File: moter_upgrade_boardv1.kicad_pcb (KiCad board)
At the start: 2 copper layers, 55 parts, among them J2 Conn_01x03_Socket, J3 Conn_01x02_Socket, J4 Conn_01x02_Socket, J5 Conn_01x02_Socket, J6 Conn_01x02_Socket, J7 Conn_ST_STDC14, J8 Conn_01x05_Socket, J9 USB_C_Receptacle_USB2.0_16P, SW1 SW_SPDT, SW2 SW_Push, SW3 SW_Wuerth_450301014042, U1 BD33FC0FP, U2 TLP785, U3 TLP785, U4 STM32H523CCTx, U5 MCP2562-E-P, U6 CH340E, U7 BD33FC0FP

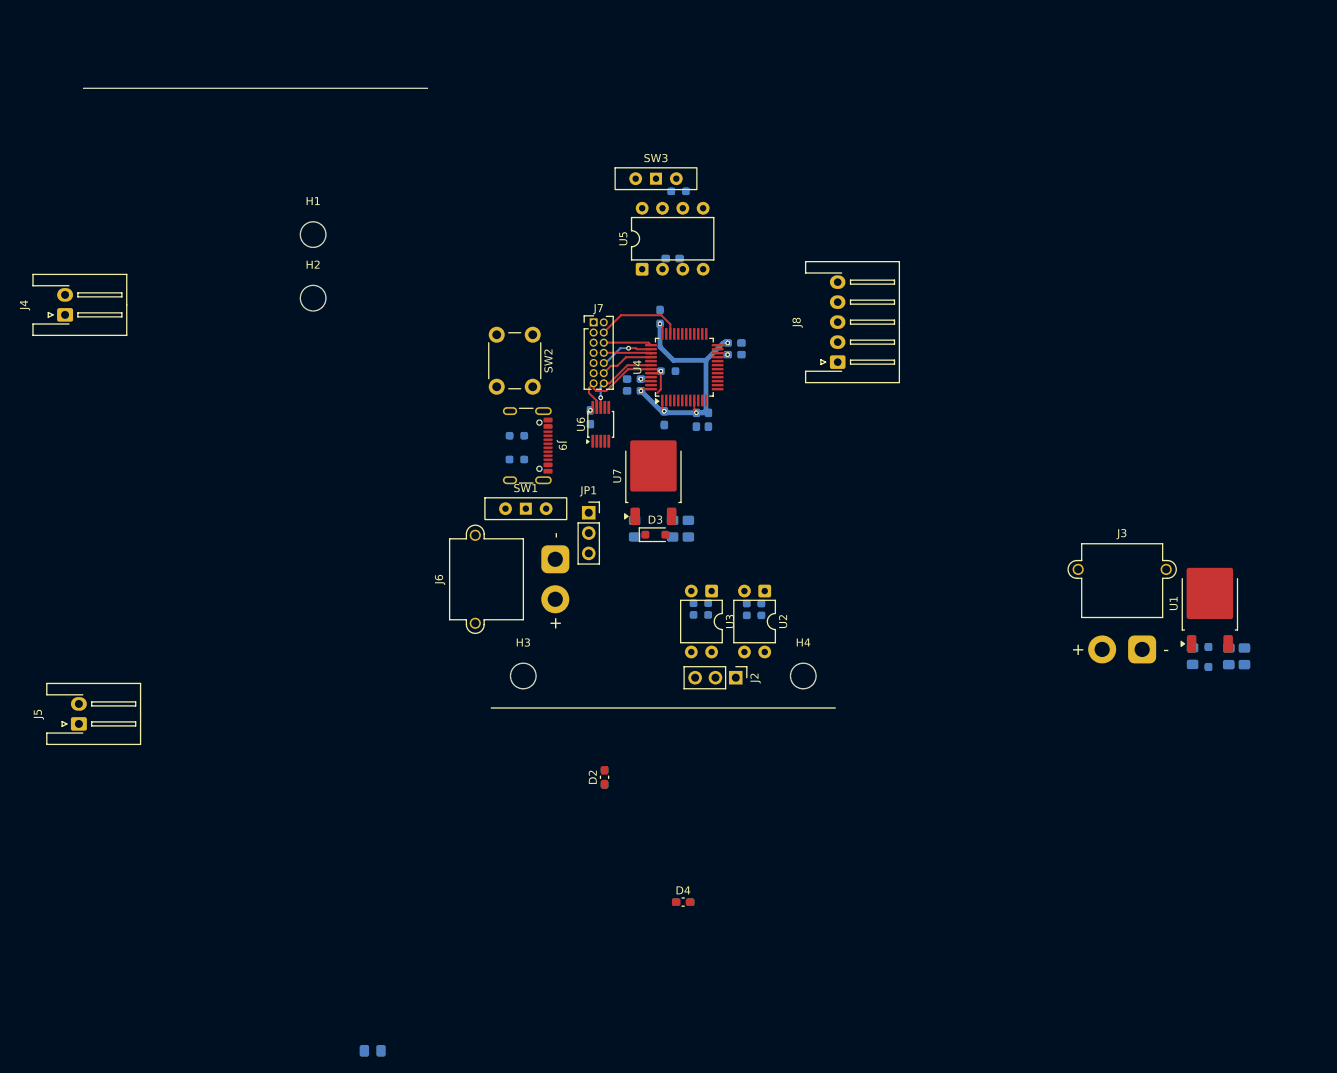
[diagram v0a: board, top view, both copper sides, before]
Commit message: 基本構成の大幅変更(マイコンも変わった
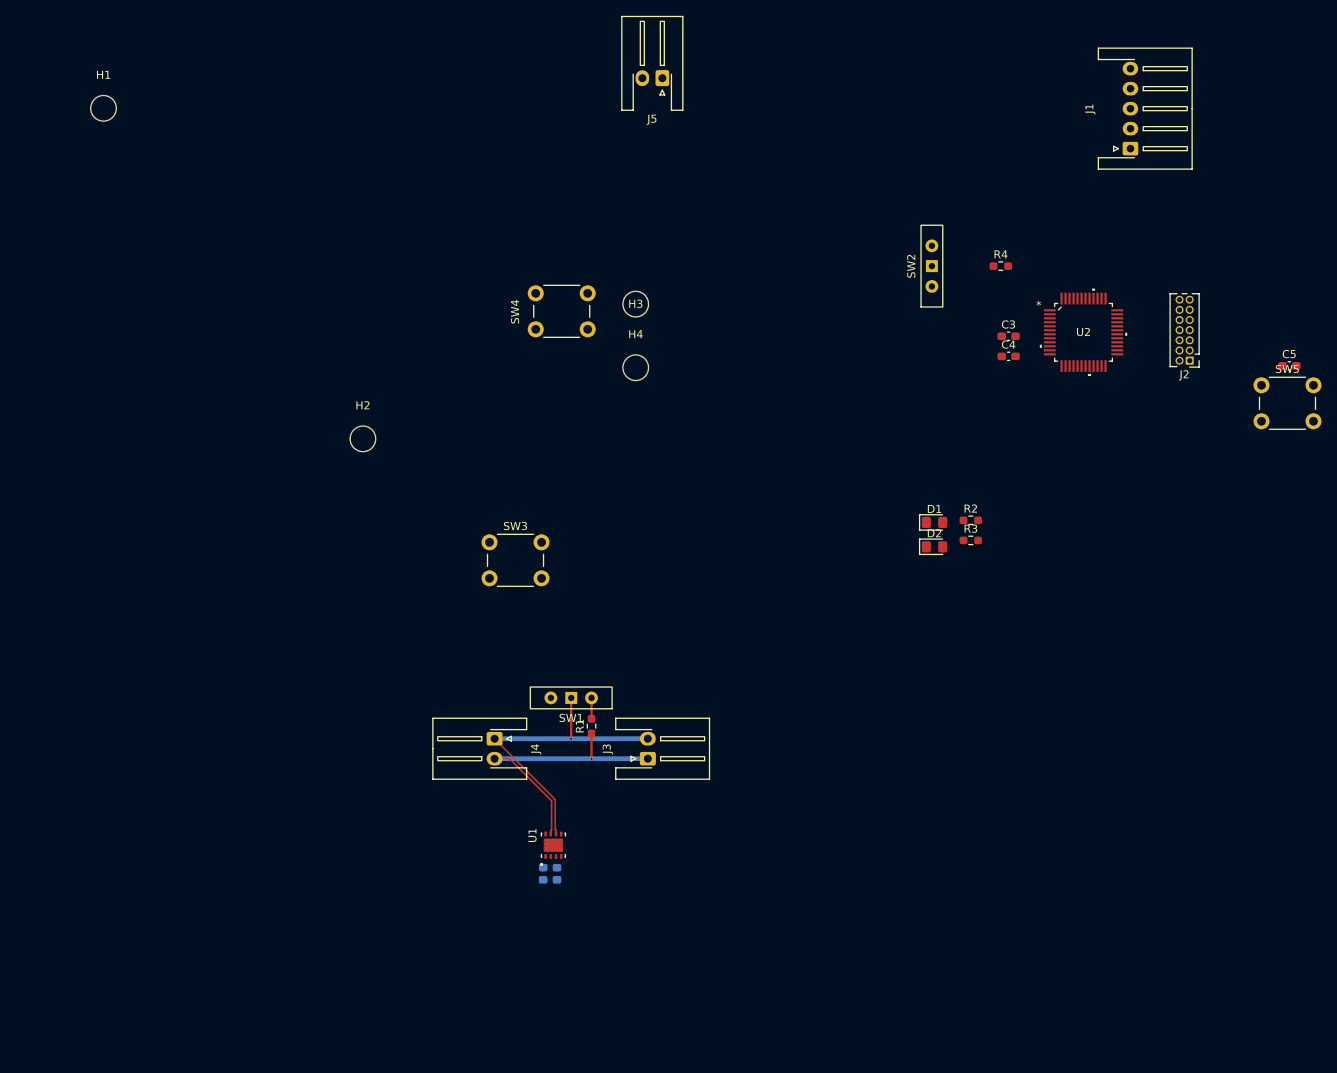
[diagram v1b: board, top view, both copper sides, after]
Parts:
- removed C10, C6, C7, C8: 0.1uF, Capacitor_SMD:C_0603_1608Metric_Pad1.08x0.95mm_HandSolder
- removed C11, C13: 0.1uf, Capacitor_SMD:C_0603_1608Metric_Pad1.08x0.95mm_HandSolder
- removed C12, C14: 1uf, Capacitor_SMD:C_0603_1608Metric_Pad1.08x0.95mm_HandSolder
- removed C15, C16: 4.7μF, Capacitor_SMD:C_0805_2012Metric_Pad1.18x1.45mm_HandSolder
- removed C17: 22μF, Capacitor_SMD:C_0805_2012Metric_Pad1.18x1.45mm_HandSolder
- removed C9: 4.7uf, Capacitor_SMD:C_0805_2012Metric_Pad1.18x1.45mm_HandSolder
- removed D3: D_Shockley, Diode_SMD:D_SOD-323_HandSoldering
- removed D4: LED_RED, Capacitor_SMD:C_0603_1608Metric_Pad1.08x0.95mm_HandSolder
- removed J6: Conn_01x02_Socket, Connector_AMASS:AMASS_XT30PW-M_1x02_P2.50mm_Horizontal
- removed J7: Conn_ST_STDC14, Connector_PinHeader_1.27mm:PinHeader_2x07_P1.27mm_Vertical
- removed J8: Conn_01x05_Socket, Connector_JST:JST_XH_S5B-XH-A-1_1x05_P2.50mm_Horizontal
- removed J9: USB_C_Receptacle_USB2.0_16P, Connector_USB:USB_C_Receptacle_GCT_USB4105-xx-A_16P_TopMnt_Horizontal
- removed JP1: Jumper_3_Bridged12, Connector_PinSocket_2.54mm:PinSocket_1x03_P2.54mm_Vertical
- removed R10, R9: 5.1k, Resistor_SMD:R_0603_1608Metric_Pad0.98x0.95mm_HandSolder
- removed R5: 10K, Resistor_SMD:R_0603_1608Metric_Pad0.98x0.95mm_HandSolder
- removed R6: 120, Resistor_SMD:R_0603_1608Metric_Pad0.98x0.95mm_HandSolder
- removed R7, R8: 1k, Resistor_SMD:R_0603_1608Metric_Pad0.98x0.95mm_HandSolder
- removed U3: TLP785, Package_DIP:DIP-4_W7.62mm
- removed U4: STM32H523CCTx, Package_QFP:LQFP-48_7x7mm_P0.5mm
- removed U5: MCP2562-E-P, Package_DIP:DIP-8_W7.62mm
- removed U6: CH340E, Package_SO:MSOP-10_3x3mm_P0.5mm
- removed U7: BD33FC0FP, Package_TO_SOT_SMD:TO-252-2
- added J1: Conn_01x05_Socket, Connector_JST:JST_XH_S5B-XH-A-1_1x05_P2.50mm_Horizontal, F.Cu at (180.9, 57.5)
- added SW4: SW_Push, Button_Switch_THT:SW_PUSH_6mm, F.Cu at (106.5, 75.6)
- added SW5: SW_Push, Button_Switch_THT:SW_PUSH_6mm, F.Cu at (197.2, 87.1)
- C1: value 4.7μF -> 0.1uF; footprint Capacitor_SMD:C_0805_2012Metric_Pad1.18x1.45mm_HandSolder -> Capacitor_SMD:C_0603_1608Metric_Pad1.08x0.95mm_HandSolder
- C2: value 4.7μF -> 4.7uF; footprint Capacitor_SMD:C_0805_2012Metric_Pad1.18x1.45mm_HandSolder -> Capacitor_SMD:C_0603_1608Metric_Pad1.08x0.95mm_HandSolder
- C3: value 22μF -> 0.1uf; footprint Capacitor_SMD:C_0805_2012Metric_Pad1.18x1.45mm_HandSolder -> Capacitor_SMD:C_0603_1608Metric_Pad1.08x0.95mm_HandSolder; moved to F.Cu
- C4: value 2.2μF -> 1uf; moved to F.Cu
- C5: value 2.2μF -> 0.1uf; moved to F.Cu
- D1: value D_Shockley -> LED_YELLOW; footprint Diode_SMD:D_SOD-323_HandSoldering -> Diode_SMD:D_0805_2012Metric_Pad1.15x1.40mm_HandSolder; moved to F.Cu
- D2: value LED_GREEN -> LED_Green; footprint Capacitor_SMD:C_0603_1608Metric_Pad1.08x0.95mm_HandSolder -> Diode_SMD:D_0805_2012Metric_Pad1.15x1.40mm_HandSolder
- J2: value Conn_01x03_Socket -> Conn_ST_STDC14; footprint Connector_PinHeader_2.54mm:PinHeader_1x03_P2.54mm_Vertical -> Connector_PinHeader_1.27mm:PinHeader_2x07_P1.27mm_Vertical
- J3: footprint Connector_AMASS:AMASS_XT30PW-M_1x02_P2.50mm_Horizontal -> Connector_JST:JST_XH_S2B-XH-A-1_1x02_P2.50mm_Horizontal
- R1: value 68 -> 120; moved to F.Cu
- R2: value 68 -> 1k; moved to F.Cu
- R3: moved to F.Cu
- R4: value 1k -> 10k; moved to F.Cu
- SW1: value SW_SPDT -> SW_Wuerth_450301014042
- SW2: value SW_Push -> SW_SPDT; footprint Button_Switch_THT:SW_PUSH_6mm -> Button_Switch_THT:SW_Slide-03_Wuerth-WS-SLTV_10x2.5x6.4_P2.54mm
- SW3: value SW_Wuerth_450301014042 -> SW_Push; footprint Button_Switch_THT:SW_Slide-03_Wuerth-WS-SLTV_10x2.5x6.4_P2.54mm -> Button_Switch_THT:SW_PUSH_6mm
- U1: value BD33FC0FP -> TCAN3414DRBR; footprint Package_TO_SOT_SMD:TO-252-2 -> TCAN3414DRBR:XCVR_TCAN3414DRBR
- U2: value TLP785 -> STM32C092CBT6; footprint Package_DIP:DIP-4_W7.62mm -> stm32c092cbt6:LQFP48_STM
- moved G*** 112.0 mm to (138.3, 150.3)
- moved J5 108.8 mm to (122.3, 48.7), turned to 180 degrees
- moved C2 89.3 mm to (108.3, 148.9), turned to 0 degrees
- moved U1 87.4 mm to (108.7, 144.6)
- moved C1 84.6 mm to (108.3, 147.4), turned to 0 degrees
- moved C5 81.9 mm to (200.7, 84.7)
- moved J4 75.4 mm to (101.4, 131.3), turned to -90 degrees
- moved J2 69.2 mm to (188.3, 84.0), turned to 180 degrees
- moved J3 63.3 mm to (120.5, 133.8), turned to 90 degrees
- moved R4 56.4 mm to (164.7, 72.2)
- moved U2 51.3 mm to (175.0, 80.5), turned to 0 degrees
- moved SW2 50.6 mm to (156.0, 72.2), turned to 90 degrees
- moved D2 50.3 mm to (156.4, 107.3), turned to 0 degrees
- moved SW3 50.0 mm to (100.8, 106.8)
- moved C3 49.7 mm to (165.6, 81.0), turned to 0 degrees
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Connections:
- C1 pad 1: +24V -> GND
- C1 pad 2: GND1 -> +3.3V
- C2 pad 1: +3V3 -> GND
- C2 pad 2: GND1 -> +3.3V
- C3 pad 1: +3V3 -> +3.3V
- C3 pad 2: GND1 -> GND
- C4 pad 1: GND -> +3.3V
- C4 pad 2: Net-(C4-Pad2) -> GND
- C5 pad 1: GND -> nrst
- C5 pad 2: Net-(C5-Pad2) -> GND
- D1 pad 1: +24V -> Net-(D1-K)
- D1 pad 2: +3V3 -> Net-(D1-A)
- J2 pad 1: Net-(J2-Pin_1) -> unconnected-(J2-NC-Pad1)
- J2 pad 2: Net-(J2-Pin_2) -> unconnected-(J2-NC-Pad2)
- J2 pad 3: GND1 -> +3.3V
- J3 pad 1: GND1 -> CAN1_+
- J3 pad 2: +24V -> CAN1_-
- J4 pad 1: CAN_L -> CAN1_-
- J4 pad 2: CAN_H -> CAN1_+
- J5 pad 1: CAN_L -> GND
- J5 pad 2: CAN_H -> +3.3V
- R1 pad 1: dir to moter -> CAN1_+
- R1 pad 2: Net-(R1-Pad2) -> CAN1R
- R2 pad 1: wm to moter -> GND
- R2 pad 2: Net-(R2-Pad2) -> Net-(D1-K)
- R3 pad 2: Net-(R1-Pad2) -> Net-(D2-K)
- R4 pad 1: GND -> swclk
- R4 pad 2: Net-(R2-Pad2) -> GND
- SW1 pad 1: GND -> CAN1_-
- SW1 pad 2: BOOT0 -> CAN1R
- SW2 pad 1: nrst -> GND
- SW2 pad 2: GND -> BOOT0
- SW3 pad 1: CAN_H -> /ma
- SW3 pad 2: unconnected-(SW3-C-Pad2) -> GND
- U1 pad 1: +24V -> CAN1tx
- U1 pad 2: GND1 -> GND
- U1 pad 3: +3V3 -> +3.3V
- U2 pad 1: Net-(R1-Pad2) -> unconnected-(U2-PC13-Pad1)
- U2 pad 2: GND -> unconnected-(U2-PC14-OSCX_IN-Pad2)
- U2 pad 3: Net-(J2-Pin_1) -> unconnected-(U2-PC15-OSCX_OUT-Pad3)
- U2 pad 4: +3V3 -> unconnected-(U2-PF3-Pad4)
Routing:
- net CAN1_-: track 0.00 -> 39.5 mm, vias 0 -> 1
- net +3.3V: track 37.7 -> 0.00 mm, vias 5 -> 0
- net CAN1_+: track 0.00 -> 36.0 mm, vias 0 -> 1
- net uart1-rx: track 12.7 -> 0.00 mm
- net swdio: track 10.9 -> 0.00 mm
- net uart1-tx: track 10.0 -> 0.00 mm, vias 1 -> 0
- net trst: track 6.73 -> 0.00 mm
- net jtdi: track 6.73 -> 0.00 mm, vias 1 -> 0
- net swclk: track 6.04 -> 0.00 mm
- net swo: track 6.01 -> 0.00 mm
- net BOOT0: track 4.28 -> 0.00 mm, vias 1 -> 0
- net CAN1R: track 0.00 -> 2.54 mm
- net Net-(C5-Pad2): track 1.38 -> 0.00 mm, vias 1 -> 0
- net Net-(C4-Pad2): track 1.33 -> 0.00 mm, vias 1 -> 0
- net Net-(U6-V3): track 0.48 -> 0.00 mm, vias 1 -> 0

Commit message: ver2完成発注(データ同梱)
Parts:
- removed the SW2 at (156.0, 72.2)
- added J6: Conn_01x03_Pin, TerminalBlock_RND:TerminalBlock_RND_205-00233_1x03_P5.08mm_Horizontal, F.Cu at (73.1, 104.0)
- added R5: 10k, Resistor_SMD:R_0805_2012Metric, B.Cu at (77.1, 83.8)
- added R6: 10k, Resistor_SMD:R_0805_2012Metric, B.Cu at (68.4, 84.8)
- added R7: 10k, Resistor_SMD:R_0805_2012Metric, B.Cu at (77.1, 81.9)
- added R8: 10k, Resistor_SMD:R_0805_2012Metric, F.Cu at (95.4, 75.7)
- C3, C4, C5, R1, R2, R3: moved to B.Cu
- R4: footprint Resistor_SMD:R_0603_1608Metric_Pad0.98x0.95mm_HandSolder -> Resistor_SMD:R_0805_2012Metric; moved to B.Cu
- moved C5 139.7 mm to (61.0, 85.1), turned to 90 degrees
- moved SW4 138.0 mm to (59.2, 87.2), turned to 180 degrees
- moved G*** 106.3 mm to (69.8, 69.0)
- moved U2 98.8 mm to (76.2, 81.8)
- moved C4 96.8 mm to (68.8, 82.2), turned to -90 degrees
- moved J1 96.4 mm to (85.0, 67.8), turned to 180 degrees
- moved J2 95.4 mm to (93.3, 75.0), turned to -90 degrees
- moved C3 95.4 mm to (70.3, 82.2), turned to -90 degrees
- moved R4 87.3 mm to (77.6, 78.7), turned to 180 degrees
- moved R3 81.2 mm to (80.0, 100.0)
- moved D2 76.7 mm to (80.0, 100.0), turned to 180 degrees
- moved R2 75.0 mm to (86.0, 100.0)
- moved H3 73.2 mm to (52.5, 107.5)
- moved C2 70.6 mm to (76.9, 85.7), turned to 180 degrees
- moved D1 70.5 mm to (86.0, 100.0), turned to 180 degrees
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- renumbered SW3 to SW2, SW4 to SW3, SW5 to SW4
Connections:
- U2 pad 23: unconnected-(U2-PB11-Pad23) -> Net-(D2-A)
- U2 pad 24: unconnected-(U2-PB12-Pad24) -> Net-(D1-A)
- U2 pad 25: unconnected-(U2-PB13-Pad25) -> /mb
- U2 pad 26: unconnected-(U2-PB14-Pad26) -> /ma
- U2 pad 39: /ma -> unconnected-(U2-PD1-Pad39)
- U2 pad 40: /mb -> unconnected-(U2-PD2-Pad40)
- U2 pad 47: Net-(D1-A) -> unconnected-(U2-PB8-Pad47)
- U2 pad 48: Net-(D2-A) -> unconnected-(U2-PB9-Pad48)
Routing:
- net +3.3V: track 0.00 -> 80.3 mm, vias 0 -> 3
- net GND: track 0.00 -> 58.8 mm, vias 0 -> 85
- net nrst: track 0.00 -> 32.5 mm, vias 0 -> 2
- net /mb: track 0.00 -> 29.5 mm, vias 0 -> 1
- net dir to moter: track 0.00 -> 25.8 mm
- net pwm to moter: track 0.00 -> 25.5 mm
- net swdio: track 0.00 -> 18.3 mm
- net Net-(D1-A): track 0.00 -> 16.5 mm, vias 0 -> 2
- net en-b: track 0.00 -> 15.7 mm
- net Net-(D2-A): track 0.00 -> 14.3 mm
- net /ma: track 0.00 -> 13.6 mm, vias 0 -> 1
- net swclk: track 0.00 -> 13.3 mm, vias 0 -> 1
- net en-a: track 0.00 -> 12.0 mm
- net strx: track 0.00 -> 10.9 mm, vias 0 -> 1
- net sttx: track 0.00 -> 10.1 mm, vias 0 -> 1
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- added copper zone on B.Cu, net GND
- added copper zone on F.Cu, net GND
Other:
- board outline added: 52 x 50 mm
